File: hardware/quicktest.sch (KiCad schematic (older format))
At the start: 23 parts

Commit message: added more to the schematic, filled in push buttons, mpu-9250
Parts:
- removed SW? (x3): SW_DIP_x02, symbol SW_DIP_x02
- added R? (x3): 1K, symbol R_Small
- added SW? (x3): SW_Push, symbol SW_Push
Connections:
- net labels added: FS, PB0, PB1, PB2
- wire segments 73 -> 91
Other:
- note added: "I2C 0x69\n(0xD2/0xD3)"
- moved on the sheet: BT?, C?, J?, R?

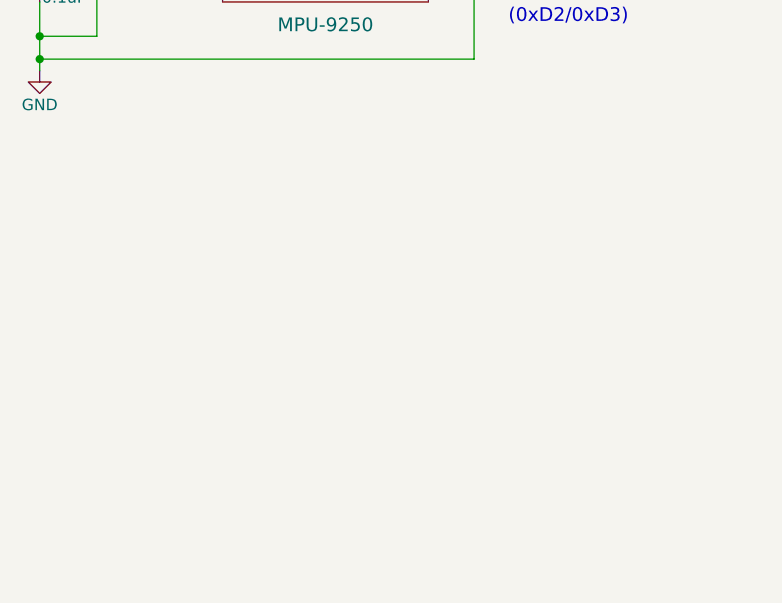
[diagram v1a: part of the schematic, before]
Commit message: adding a potential oled component
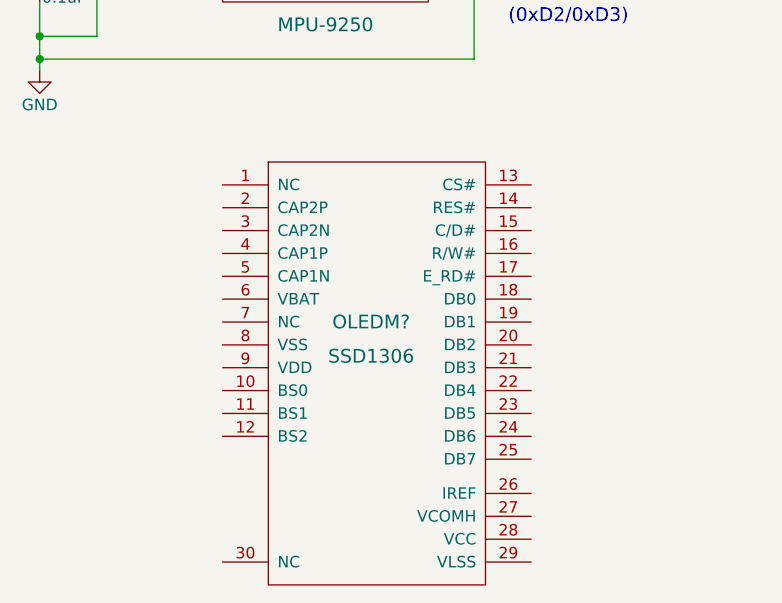
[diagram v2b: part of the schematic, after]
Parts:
- added OLEDM?: SSD1306, symbol SSD1306
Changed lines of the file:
@@
 LIBS:mpu-9250
 LIBS:maxim
+LIBS:mod-oled-128x64-cache
+LIBS:oled
 LIBS:quicktest-cache
 EELAYER 25 0
@@
 Text GLabel 1500 4450 0    60   Input ~ 0
 FS
+$Comp
+L SSD1306 OLEDM?
+U 1 1 597388E9
+P 2450 6400
+F 0 "OLEDM?" H 2350 6550 60  0000 C CNN
+F 1 "SSD1306" H 2350 6400 60  0000 C CNN
+F 2 "" H 2450 6400 60  0000 C CNN
+F 3 "" H 2450 6400 60  0000 C CNN
+	1    2450 6400
+	1    0    0    -1
+$EndComp
 $EndSCHEMATC

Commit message: finished up the oled. adding some usb->ftdi support...need more research on this
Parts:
- added C? (x4): 1uF, symbol C_Small
- added C?: 2.2uF, symbol C_Small
- added C?: 4.7uF, symbol C_Small
- added CON?: USB-MICRO-B, symbol USB-MICRO-B
- added R?: 390K, symbol R_Small
- added U?: FTS31XS-U-SSOP, symbol FTS31XS-U-SSOP
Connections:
- net +3V3: now also OLEDM?.6 (VBAT), OLEDM?.9 (VDD), C?.1, C?.1
- net CS: now also OLEDM?.13 (CS#)
- net FS: now also U?.2 ((PCINT20/XCK/T0)PD4); no longer U?.23 ((PCINT8/ADC0)PC0)
- net GND: now also OLEDM?.1 (NC), OLEDM?.10 (BS0), OLEDM?.11 (BS1), OLEDM?.12 (BS2), OLEDM?.16 (R/W#), OLEDM?.17 (E_RD#), OLEDM?.21 (DB3), OLEDM?.22 (DB4), OLEDM?.23 (DB5), OLEDM?.24 (DB6), OLEDM?.25 (DB7), OLEDM?.29 (VLSS), OLEDM?.30 (NC), OLEDM?.8 (VSS), C?.2, C?.2, C?.2, C?.2, R?.2
- net MOSI: now also OLEDM?.19 (DB1)
- net PB0: now also U?.9 ((PCINT21/OC0B/T1)PD5); no longer U?.24 ((PCINT9/ADC1)PC1)
- net PB1: now also U?.10 ((PCINT22/OC0A/AIN0)PD6); no longer U?.25 ((PCINT10/ADC2)PC2)
- net PB2: now also U?.11 ((PCINT23/AIN1)PD7); no longer U?.26 ((PCINT11/ADC3)PC3)
- net SCK: now also OLEDM?.18 (DB0)
- net VIB: now also U?.23 ((PCINT8/ADC0)PC0)
- net D8: now reaches U?.12 ((PCINT0/CLKO/ICP1)PB0)
- net D8: now also OLEDM?.15 (C/D#)
- net D9: now reaches U?.13 ((PCINT1/OC1A)PB1)
- net D9: now also OLEDM?.14 (RES#)
- net MISO: now reaches U?.16 ((PCINT4/MISO)PB4)
- net A6: now reaches U?.19 (ADC6)
- net A7: now reaches U?.22 (ADC7)
- net at OLEDM?.2 (CAP2P): now also C?.1
- net at OLEDM?.26 (IREF): now also R?.1
- net at OLEDM?.27 (VCOMH): now also C?.1
- net at OLEDM?.28 (VCC): now also C?.1
- net at OLEDM?.3 (CAP2N): now also C?.2
- net at OLEDM?.4 (CAP1P): now also C?.1
- net at OLEDM?.5 (CAP1N): now also C?.2
- new net A1: U?.24 ((PCINT9/ADC1)PC1)
- new net A2: U?.25 ((PCINT10/ADC2)PC2)
- new net A3: U?.26 ((PCINT11/ADC3)PC3)
- no-connect marks 3 -> 5
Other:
- note added: "Accel/Gyro/Magn"
- note added: "OLED 128x64"
- note added: "Pushbuttons (Active High)"
- note added: "RTC"
- note added: "Vibration Motor"
- moved on the sheet: BT?, C?, D?, J?, OLEDM?, Q?, R?, SW?, U?, Y?

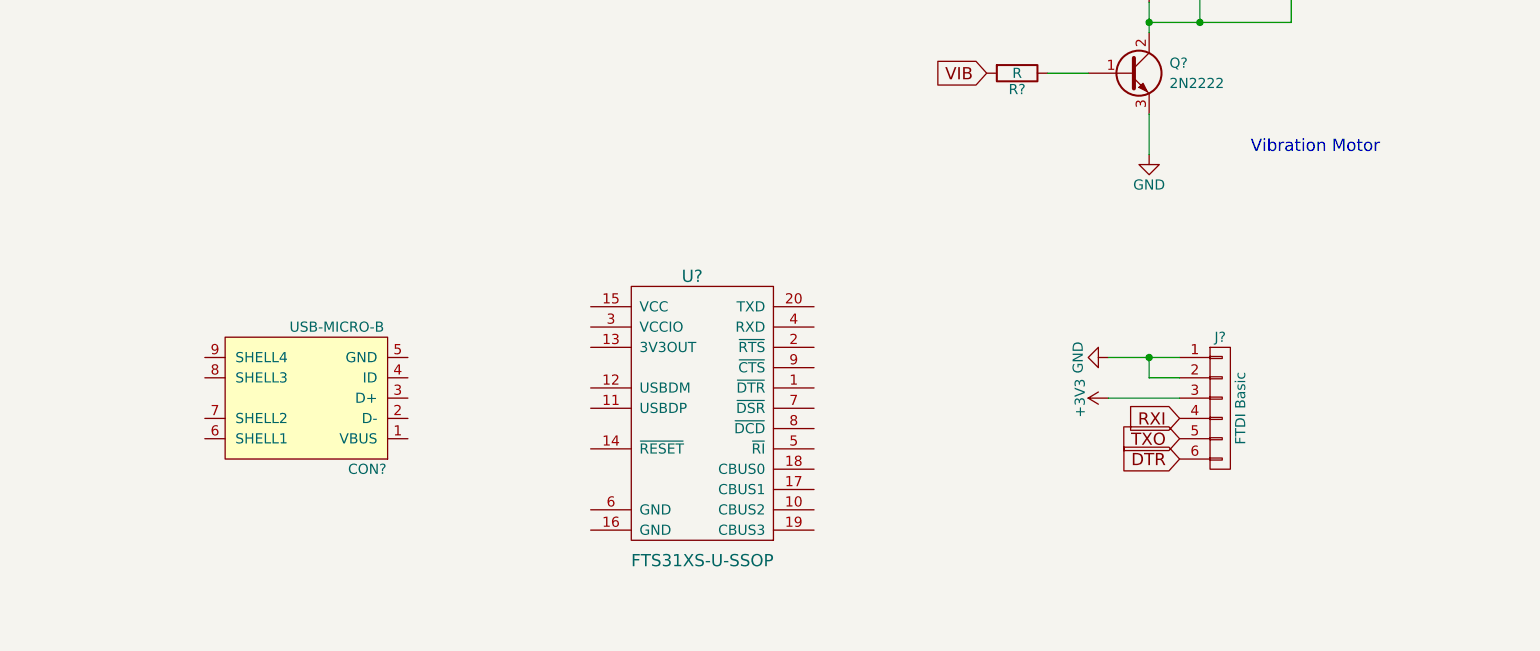
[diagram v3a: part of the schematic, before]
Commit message: added in the wiring for the USB->FTDI. it *should* also power the micro when the usb is plugged in
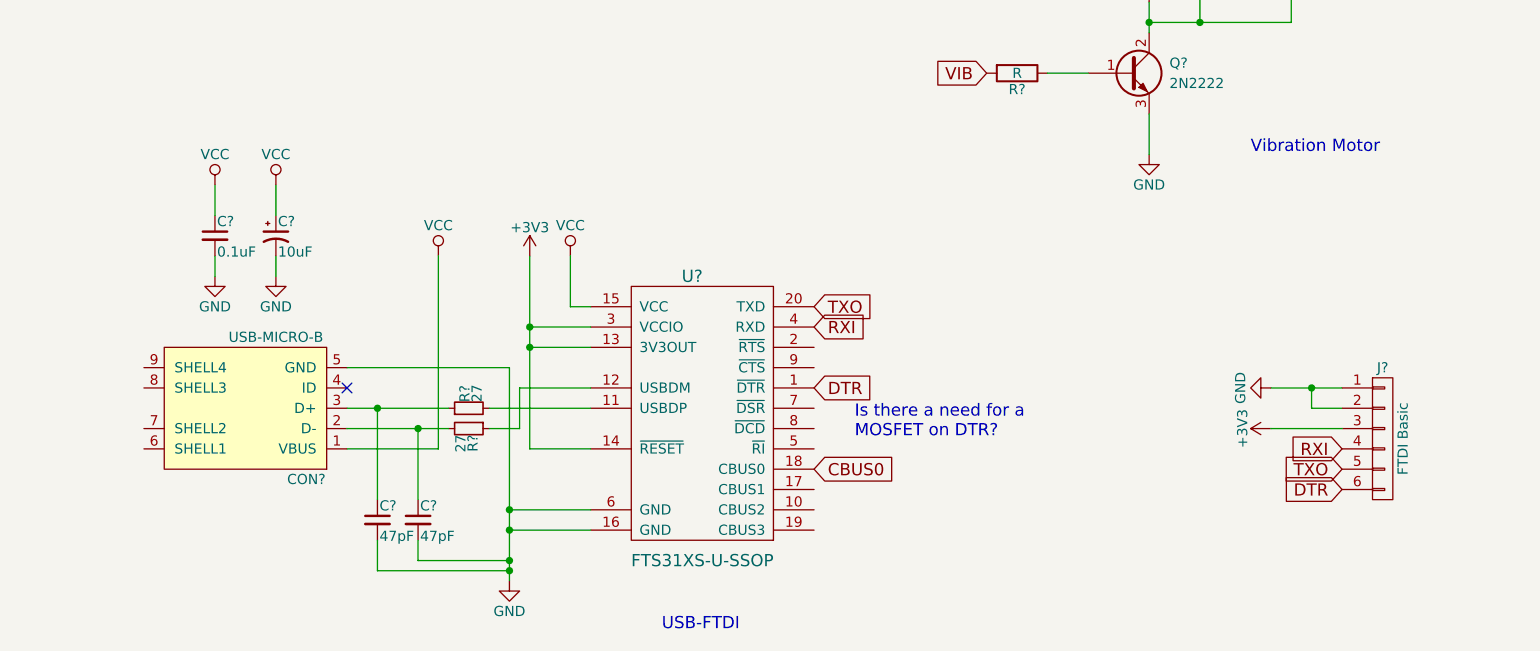
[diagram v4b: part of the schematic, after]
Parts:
- added C? (x2): 47pF, symbol C_Small
- added C?: 0.1uF, symbol C_Small
- added C?: 10uF, symbol CP1_Small
- added R? (x2): 27, symbol R_Small
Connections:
- net +3V3: now also U?.13 (3V3OUT), U?.14 (~RESET), U?.3 (VCCIO)
- net DTR: now also U?.1 (~DTR)
- net GND: now also CON?.5 (GND), U?.16 (GND), U?.6 (GND), C?.2, C?.2, C?.2, C?.2
- net RXI: now also U?.4 (RXD)
- net TXO: now also U?.20 (TXD)
- net at U?.11 (USBDP): now also R?.2
- net at U?.12 (USBDM): now also R?.1
- net VCC: now reaches U?.15 (VCC)
- net VCC: now also CON?.1 (VBUS), C?.1, C?.1
- net CBUS0: now reaches U?.18 (CBUS0)
- net at CON?.2 (D-): now also C?.1, R?.2
- net at CON?.3 (D+): now also C?.1, R?.1
- no-connect marks 5 -> 6
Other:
- note added: "Is there a need for a \nMOSFET on DTR?"
- note added: "USB-FTDI"
- moved on the sheet: CON?, J?

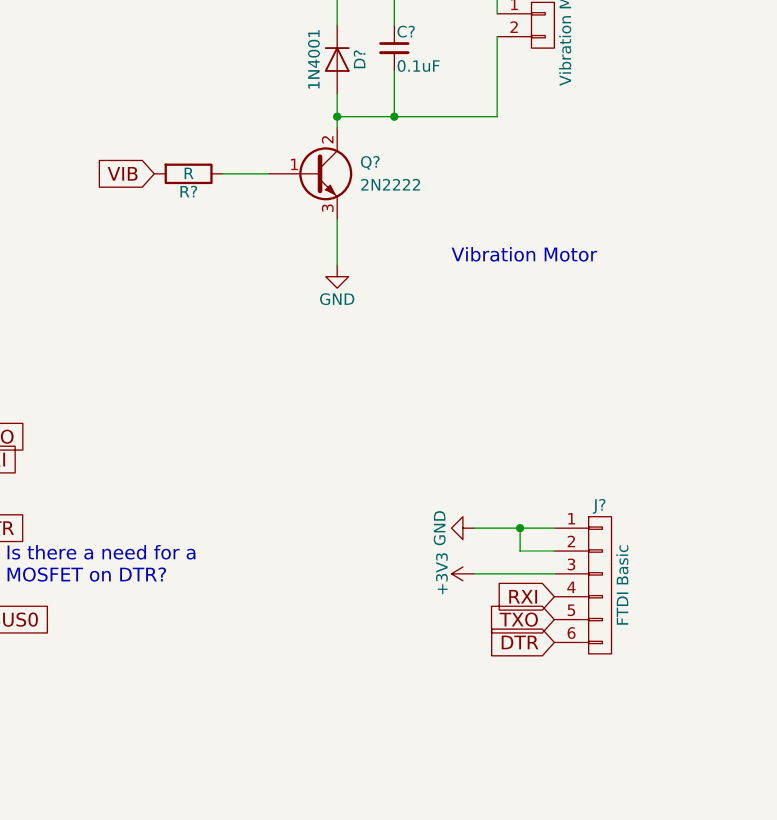
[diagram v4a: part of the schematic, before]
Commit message: a resistor value fix
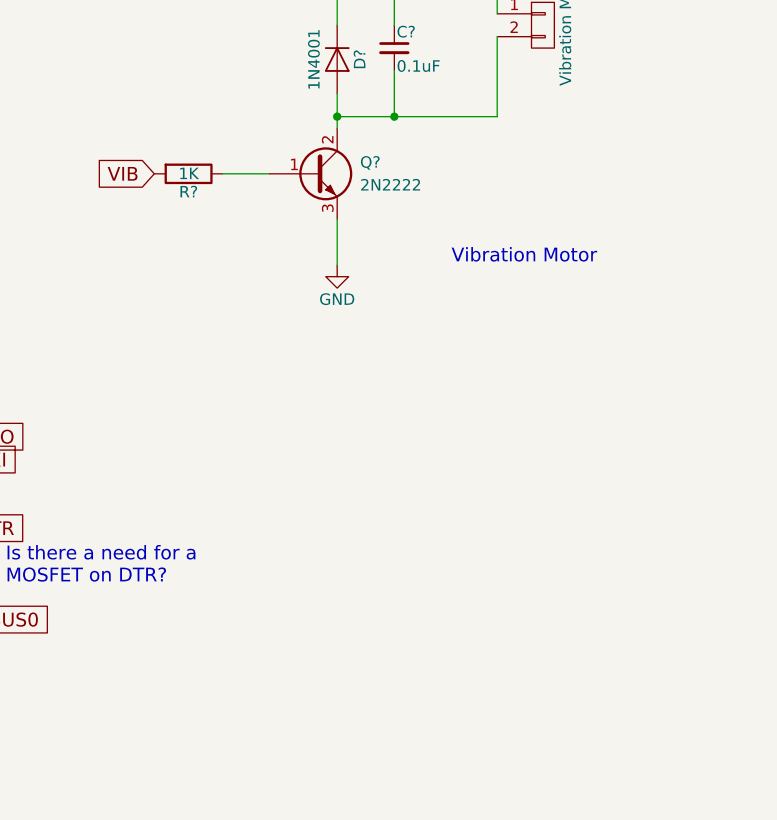
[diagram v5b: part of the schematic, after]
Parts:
- removed J?: FTDI Basic, symbol CONN_01X06
- R?: value R -> 1K
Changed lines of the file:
@@
-$EndComp
-$Comp
-L CONN_01X06 J?
-U 1 1 596E1A00
-P 15100 8800
-F 0 "J?" H 15100 9150 50  0000 C CNN
-F 1 "FTDI Basic" V 15200 8800 50  0000 C CNN
-F 2 "" H 15100 8800 50  0001 C CNN
-F 3 "" H 15100 8800 50  0001 C CNN
-	1    15100 8800
-	1    0    0    -1
-$EndComp
-Text GLabel 14900 8850 0    60   Input ~ 0
-RXI
-Text GLabel 14900 8950 0    60   Input ~ 0
-TXO
-Text GLabel 14900 9050 0    60   Input ~ 0
-DTR
-$Comp
-L GND #PWR?
-U 1 1 596E1D4E
-P 14550 8550
-F 0 "#PWR?" H 14550 8300 50  0001 C CNN
-F 1 "GND" H 14550 8400 50  0000 C CNN
-F 2 "" H 14550 8550 50  0001 C CNN
-F 3 "" H 14550 8550 50  0001 C CNN
-	1    14550 8550
-	0    1    1    0
-$EndComp
-$Comp
-L +3V3 #PWR?
-U 1 1 596E1D76
-P 14550 8750
-F 0 "#PWR?" H 14550 8600 50  0001 C CNN
-F 1 "+3V3" H 14550 8890 50  0000 C CNN
-F 2 "" H 14550 8750 50  0001 C CNN
-F 3 "" H 14550 8750 50  0001 C CNN
-	1    14550 8750
-	0    -1   -1   0
 $EndComp
 $Comp
@@
 P 13300 7000
 F 0 "R?" V 13380 7000 50  0000 C CNN
-F 1 "R" V 13300 7000 50  0000 C CNN
+F 1 "1K" V 13300 7000 50  0000 C CNN
 F 2 "" V 13230 7000 50  0001 C CNN
 F 3 "" H 13300 7000 50  0001 C CNN
@@
 Connection ~ 13050 1300
 Wire Wire Line
-	14550 8550 14900 8550
-Wire Wire Line
-	14900 8650 14750 8650
-Wire Wire Line
-	14750 8650 14750 8550
-Connection ~ 14750 8550
-Wire Wire Line
-	14900 8750 14550 8750
-Wire Wire Line
 	13850 1900 13850 1750

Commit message: made a lot of changes. used kicad library component for ft231 made sure ft231 components looked correct
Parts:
- removed C? (x2): 47pF, symbol C_Small
- removed CON?: USB-MICRO-B, symbol USB-MICRO-B
- removed R? (x2): 27, symbol R_Small
- removed U?: DS3231, Housings_SOIC:SOIC-16_7.5x10.3mm_Pitch1.27mm, symbol DS3231
- removed U?: FTS31XS-U-SSOP, symbol FTS31XS-U-SSOP
- added C? (x2): 47pF, symbol C_Small
- added C?: 0.1uF, symbol C_Small
- added J?: USB_OTG, symbol USB_OTG
- added L?: 500mA, symbol Ferrite_Bead
- added R? (x2): 27, symbol R_Small
- added U?: DS3231MZ, Housings_SOIC:SOIC-8_3.9x4.9mm_Pitch1.27mm, symbol DS3231MZ
- added U?: FT231XS, SSOP-20, symbol FT231XS
- C?: value 10uF -> 4.7uF
- Y?: value Crystal_GND2 -> 8MHz
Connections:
- net +3V3: now also U?.13 (3V3OUT), U?.14 (~RESET), U?.3 (VCCIO), U?.4 (~RST), U?.6 (VBAT)
- net CBUS0: now also U?.18 (CBUS0)
- net DTR: now also U?.1 (~DTR)
- net GND: now also C?.2, C?.2, C?.2, J?.5 (GND), U?.16 (GND), U?.2 (VCC), U?.5 (GND), U?.6 (GND)
- net INT0: now also U?.3 (~INT~/SQW)
- net RXI: now also U?.4 (RXD)
- net SCL: now also U?.8 (SCL)
- net SDA: now also U?.7 (SDA)
- net TXO: now also U?.20 (TXD)
- net VCC renamed +5V
- net +5V: now also L?.1, U?.15 (VCC)
- new net: C?.1, J?.1 (VBUS), L?.2
- new net: R?.1, U?.11 (USBDP)
- new net: R?.2, U?.12 (USBDM)
- new net: C?.1, J?.2 (D-), R?.1
- new net: C?.1, J?.3 (D+), R?.2
- new net RTS: U?.2 (~RTS)
- new net SHIELD: J?.6 (Shield)
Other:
- note added: "Do internal resistors and Active Low?\nsave on components..."
- note added: "From Atmega328p"
- note added: "From OLED"
- note added: "May need caps around the XTAL"
- note removed: "Is there a need for a \nMOSFET on DTR?"
- moved on the sheet: BT?, C?, R?
